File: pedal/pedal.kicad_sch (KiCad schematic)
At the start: 29 parts, among them J1 AudioJack3, J2 AudioJack3, J3 Micro SD, J4 USB_B_Micro, J5 Debug, U2 PCM3060, U3 LP2985-3.3, U4 TPS62170DSG, U5 STM32H750IBTx

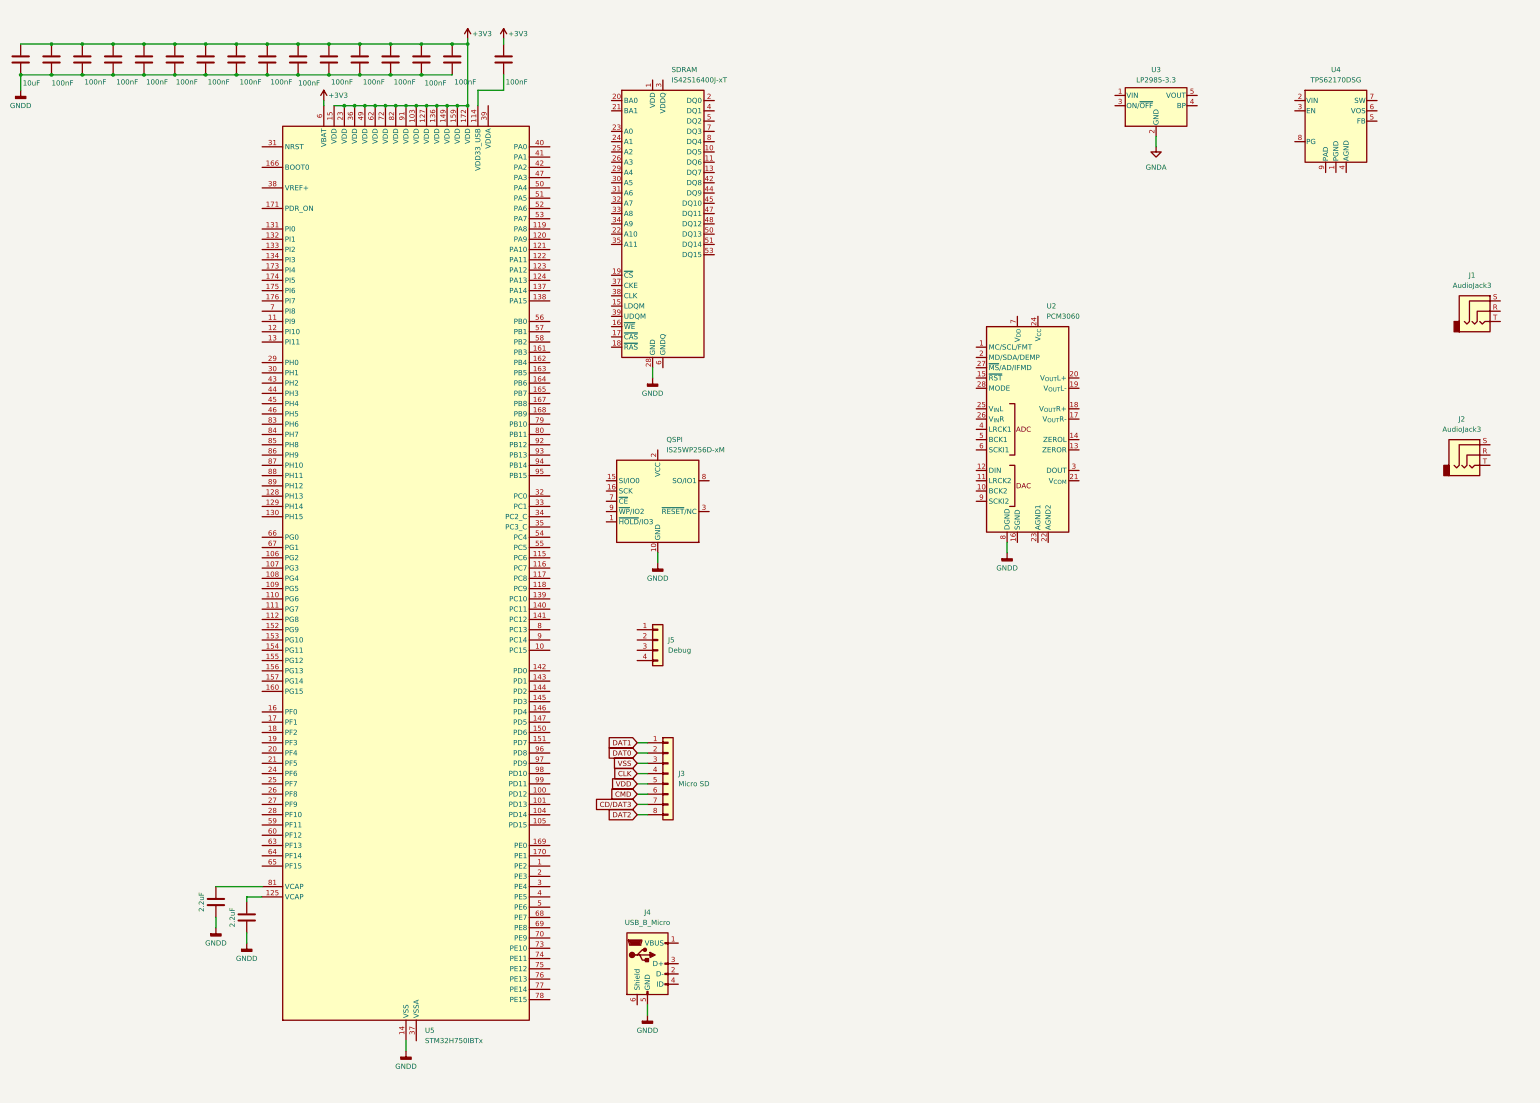
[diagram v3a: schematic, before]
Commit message: ferrite bead & buses with SDRAM
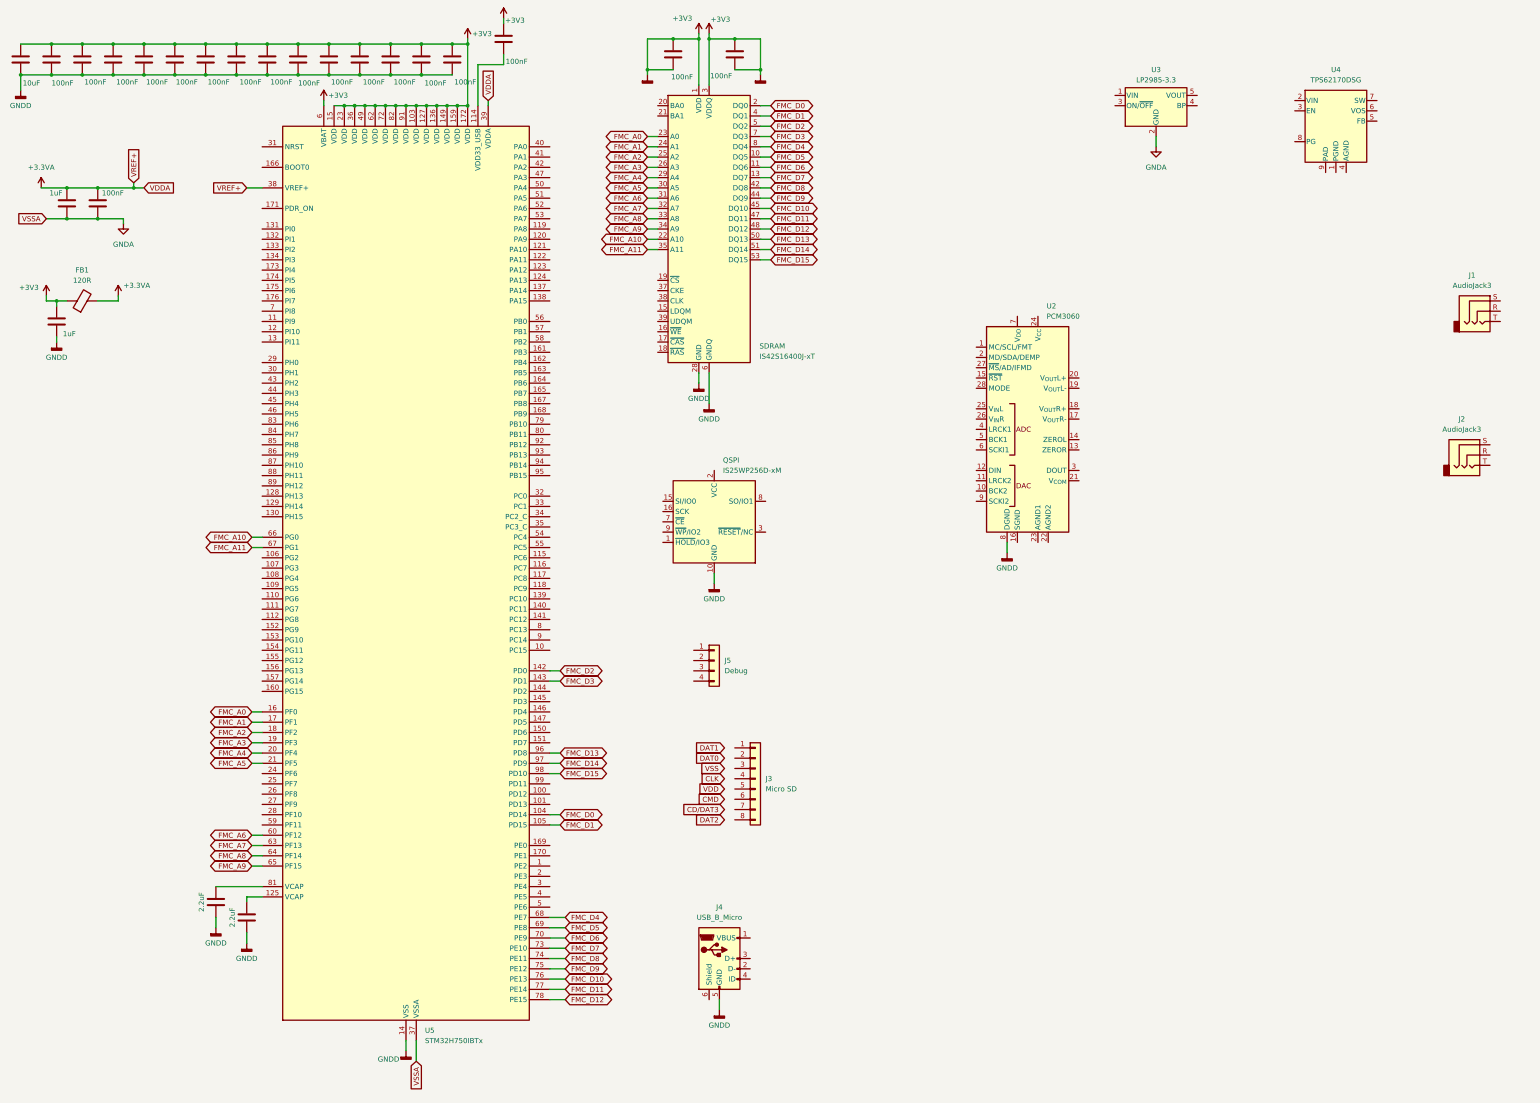
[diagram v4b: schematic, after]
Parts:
- added C19, C21: 1uF, symbol Device:C
- added C20, C22, C23: 100nF, symbol Device:C
- added FB1: 120R, symbol Device:FerriteBead
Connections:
- net GNDD is gone; now on net +3V3: C1.1, C10.2, C11.2, C12.2, C13.2, C14.2, C15.2, C16.2, C17.2, C2.1, C3.2, C4.2, C5.2, C6.2, C7.2, C8.2, C9.2, J4.5 (GND), QSPI.10 (GND), SDRAM.28 (GND), SDRAM.41 (GND), SDRAM.54 (GND), U2.8 (DGND), U5.102 (VSS), U5.113 (VSS), U5.126 (VSS), U5.135 (VSS), U5.14 (VSS), U5.148 (VSS), U5.158 (VSS), U5.22 (VSS), U5.48 (VSS), U5.61 (VSS), U5.71 (VSS), U5.90 (VSS)
- net +3V3: now also SDRAM.1 (VDD), SDRAM.12 (GNDQ), SDRAM.14 (VDD), SDRAM.27 (VDD), SDRAM.3 (VDDQ), SDRAM.43 (VDDQ), SDRAM.46 (GNDQ), SDRAM.49 (VDDQ), SDRAM.52 (GNDQ), SDRAM.6 (GNDQ), SDRAM.9 (VDDQ), C21.1, C21.2, C22.1, C22.2, C23.1, C23.2, FB1.1
- net CD/DAT3: no longer J3.7 (Pin_7)
- net CLK: no longer J3.4 (Pin_4)
- net CMD: no longer J3.6 (Pin_6)
- net DAT0: no longer J3.2 (Pin_2)
- net DAT1: no longer J3.1 (Pin_1)
- net DAT2: no longer J3.8 (Pin_8)
- net GNDA: now also U5.37 (VSSA), C19.2, C20.2
- net VDD: no longer J3.5 (Pin_5)
- net VSS: no longer J3.3 (Pin_3)
- net FMC_D5: now reaches SDRAM.10 (DQ5)
- net FMC_D5: now also U5.69 (PE8)
- net FMC_D6: now reaches SDRAM.11 (DQ6)
- net FMC_D6: now also U5.70 (PE9)
- net FMC_D7: now reaches SDRAM.13 (DQ7)
- net FMC_D7: now also U5.73 (PE10)
- net FMC_D0: now reaches SDRAM.2 (DQ0)
- net FMC_D0: now also U5.104 (PD14)
- net FMC_A10: now reaches SDRAM.22 (A10)
- net FMC_A10: now also U5.66 (PG0)
- net FMC_A0: now reaches SDRAM.23 (A0)
- net FMC_A0: now also U5.16 (PF0)
- net FMC_A1: now reaches SDRAM.24 (A1)
- net FMC_A1: now also U5.17 (PF1)
- net FMC_A2: now reaches SDRAM.25 (A2)
- net FMC_A2: now also U5.18 (PF2)
- net FMC_A3: now reaches SDRAM.26 (A3)
- net FMC_A3: now also U5.19 (PF3)
- net FMC_A4: now reaches SDRAM.29 (A4)
- net FMC_A4: now also U5.20 (PF4)
- net FMC_A5: now reaches SDRAM.30 (A5)
- net FMC_A5: now also U5.21 (PF5)
- net FMC_A6: now reaches SDRAM.31 (A6)
- net FMC_A6: now also U5.60 (PF12)
- net FMC_A7: now reaches SDRAM.32 (A7)
- net FMC_A7: now also U5.63 (PF13)
- net FMC_A8: now reaches SDRAM.33 (A8)
- net FMC_A8: now also U5.64 (PF14)
- net FMC_A9: now reaches SDRAM.34 (A9)
- net FMC_A9: now also U5.65 (PF15)
- net FMC_A11: now reaches SDRAM.35 (A11)
- net FMC_A11: now also U5.67 (PG1)
- net FMC_D1: now reaches SDRAM.4 (DQ1)
- net FMC_D1: now also U5.105 (PD15)
- net FMC_D8: now reaches SDRAM.42 (DQ8)
- net FMC_D8: now also U5.74 (PE11)
- net FMC_D9: now reaches SDRAM.44 (DQ9)
- net FMC_D9: now also U5.75 (PE12)
- net FMC_D10: now reaches SDRAM.45 (DQ10)
- net FMC_D10: now also U5.76 (PE13)
- net FMC_D11: now reaches SDRAM.47 (DQ11)
- net FMC_D11: now also U5.77 (PE14)
- net FMC_D12: now reaches SDRAM.48 (DQ12)
- net FMC_D12: now also U5.78 (PE15)
- net FMC_D2: now reaches SDRAM.5 (DQ2)
- net FMC_D2: now also U5.142 (PD0)
- net FMC_D13: now reaches SDRAM.50 (DQ13)
- net FMC_D13: now also U5.96 (PD8)
- net FMC_D14: now reaches SDRAM.51 (DQ14)
- net FMC_D14: now also U5.97 (PD9)
- net FMC_D15: now reaches SDRAM.53 (DQ15)
- net FMC_D15: now also U5.98 (PD10)
- net FMC_D3: now reaches SDRAM.7 (DQ3)
- net FMC_D3: now also U5.143 (PD1)
- net FMC_D4: now reaches SDRAM.8 (DQ4)
- net FMC_D4: now also U5.68 (PE7)
- net +3.3VA: now reaches U5.38 (VREF+)
- net +3.3VA: now also U5.39 (VDDA), C19.1, C20.1, FB1.2
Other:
- moved on the sheet: J3, J4, J5, QSPI, SDRAM

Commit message: finish wiring SDRAM
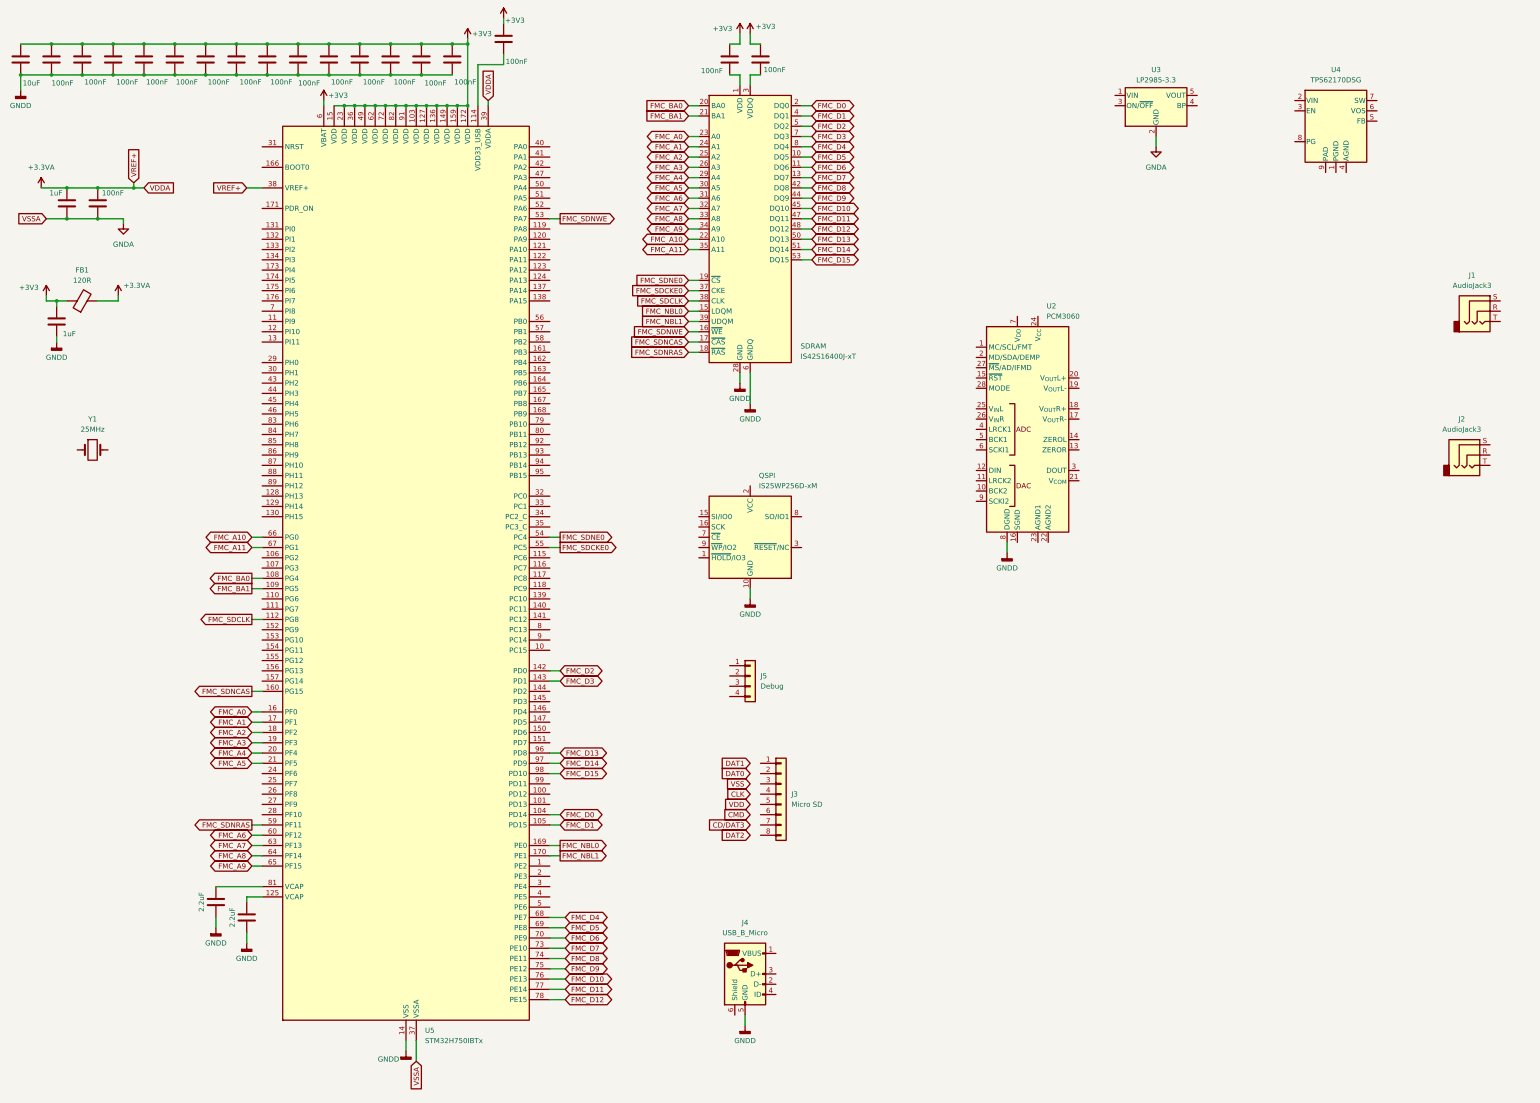
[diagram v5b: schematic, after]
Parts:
- added Y1: 25MHz, symbol Device:Crystal
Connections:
- net +3V3: no longer C1.1, C10.2, C11.2, C12.2, C13.2, C14.2, C15.2, C16.2, C17.2, C2.1, C21.2, C22.2, C23.2, C3.2, C4.2, C5.2, C6.2, C7.2, C8.2, C9.2, J4.5 (GND), QSPI.10 (GND), SDRAM.1 (VDD), SDRAM.12 (GNDQ), SDRAM.14 (VDD), SDRAM.27 (VDD), SDRAM.28 (GND), SDRAM.3 (VDDQ), SDRAM.41 (GND), SDRAM.43 (VDDQ), SDRAM.46 (GNDQ), SDRAM.49 (VDDQ), SDRAM.52 (GNDQ), SDRAM.54 (GND), SDRAM.6 (GNDQ), SDRAM.9 (VDDQ), U2.8 (DGND), U5.102 (VSS), U5.113 (VSS), U5.126 (VSS), U5.135 (VSS), U5.14 (VSS), U5.148 (VSS), U5.158 (VSS), U5.22 (VSS), U5.48 (VSS), U5.61 (VSS), U5.71 (VSS), U5.90 (VSS)
- net FMC_NBL0: now reaches SDRAM.15 (LDQM)
- net FMC_NBL0: now also U5.169 (PE0)
- net FMC_SDNWE: now reaches SDRAM.16 (~{WE})
- net FMC_SDNWE: now also U5.53 (PA7)
- net FMC_SDNCAS: now reaches SDRAM.17 (~{CAS})
- net FMC_SDNCAS: now also U5.160 (PG15)
- net FMC_SDNRAS: now reaches SDRAM.18 (~{RAS})
- net FMC_SDNRAS: now also U5.59 (PF11)
- net FMC_SDNE0: now reaches SDRAM.19 (~{CS})
- net FMC_SDNE0: now also U5.54 (PC4)
- net FMC_BA0: now reaches SDRAM.20 (BA0)
- net FMC_BA0: now also U5.108 (PG4)
- net FMC_BA1: now reaches SDRAM.21 (BA1)
- net FMC_BA1: now also U5.109 (PG5)
- net FMC_SDCKE0: now reaches SDRAM.37 (CKE)
- net FMC_SDCKE0: now also U5.55 (PC5)
- net FMC_SDCLK: now reaches SDRAM.38 (CLK)
- net FMC_SDCLK: now also U5.112 (PG8)
- net FMC_NBL1: now reaches SDRAM.39 (UDQM)
- net FMC_NBL1: now also U5.170 (PE1)
- new net: C22.2, SDRAM.1 (VDD), SDRAM.14 (VDD), SDRAM.27 (VDD)
- new net: C23.2, SDRAM.3 (VDDQ), SDRAM.43 (VDDQ), SDRAM.49 (VDDQ), SDRAM.9 (VDDQ)
- new net GNDD: C1.1, C10.2, C11.2, C12.2, C13.2, C14.2, C15.2, C16.2, C17.2, C2.1, C21.2, C3.2, C4.2, C5.2, C6.2, C7.2, C8.2, C9.2, J4.5 (GND), QSPI.10 (GND), SDRAM.12 (GNDQ), SDRAM.28 (GND), SDRAM.41 (GND), SDRAM.46 (GNDQ), SDRAM.52 (GNDQ), SDRAM.54 (GND), SDRAM.6 (GNDQ), U2.8 (DGND), U5.102 (VSS), U5.113 (VSS), U5.126 (VSS), U5.135 (VSS), U5.14 (VSS), U5.148 (VSS), U5.158 (VSS), U5.22 (VSS), U5.48 (VSS), U5.61 (VSS), U5.71 (VSS), U5.90 (VSS)
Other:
- moved on the sheet: J3, J4, J5, QSPI, SDRAM

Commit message: add external clock
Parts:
- added C24, C25: 18pF, symbol Device:C
- added R1: 10R, symbol Device:R
- added R2: 47R, symbol Device:R
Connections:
- net FMC_SDCLK: now also R1.1; no longer U5.112 (PG8)
- net GNDD: now also C24.1, C25.1
- net OSC_OUT: now reaches Y1.1
- net OSC_OUT: now also C25.2, R2.2
- net OSC_IN: now reaches Y1.2
- net OSC_IN: now also U5.29 (PH0), C24.2
- net at U5.30 (PH1): now also R2.1
- new net: R1.2, U5.112 (PG8)
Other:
- moved on the sheet: Y1

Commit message: update LDO
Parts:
- removed U3: LP2985-3.3, Package_TO_SOT_SMD:SOT-23-5, symbol Regulator_Linear:LP2985-3.3
- added C26: 10nF, symbol Device:C
- added C27: 1.0uF, symbol Device:C
- added C28: 4.7uF, symbol Device:C
- added U1: LP2985-1.8, Package_TO_SOT_SMD:SOT-23-5, symbol Regulator_Linear:LP2985-1.8
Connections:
- net +3V3: now also C27.1, U1.1 (VIN), U1.3 (ON/~{OFF})
- net GNDA: now also C26.2, C27.2, C28.2, U1.2 (GND)
- net QUADSPI_CLK: now reaches QSPI.16 (SCK)
- new net: C26.1, U1.4 (BP)
- new net +1V8: C28.1, U1.5 (VOUT)
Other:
- moved on the sheet: QSPI

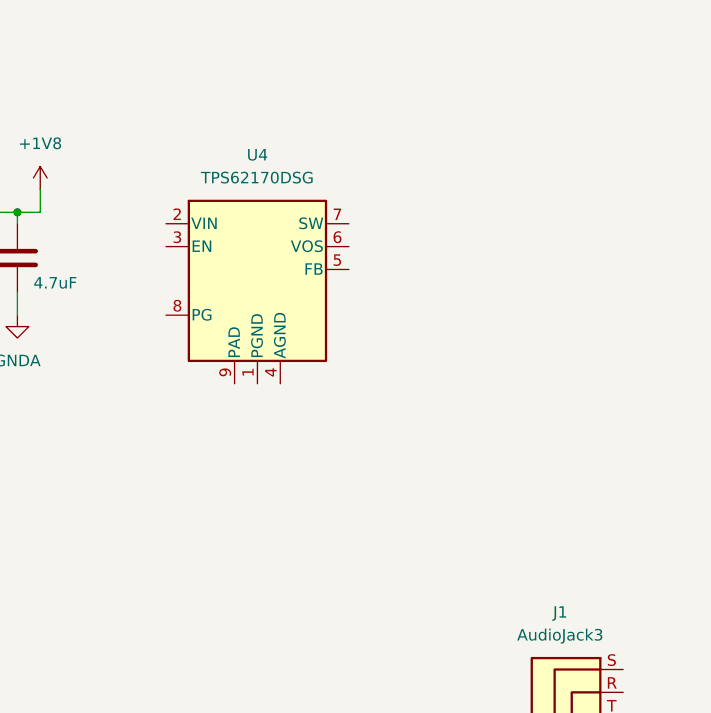
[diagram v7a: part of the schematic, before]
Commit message: update TPS62
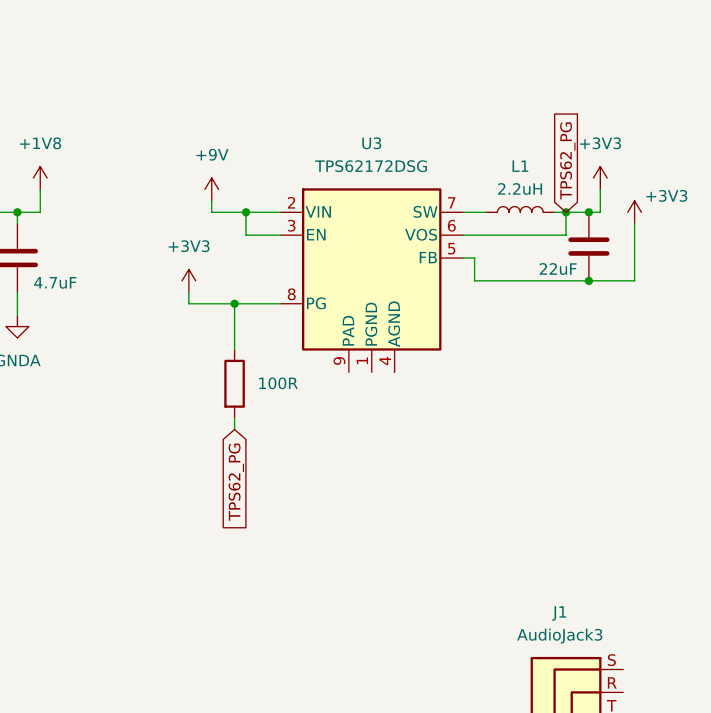
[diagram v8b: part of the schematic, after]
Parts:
- removed U4: TPS62170DSG, Package_SON:WSON-8-1EP_2x2mm_P0.5mm_EP0.9x1.6mm_ThermalVias, symbol Regulator_Switching:TPS62170DSG
- added C29: 22uF, symbol Device:C
- added L1: 2.2uH, symbol Device:L
- added R3: 100R, symbol Device:R
- added U3: TPS62172DSG, Package_SON:WSON-8-1EP_2x2mm_P0.5mm_EP0.9x1.6mm_ThermalVias, symbol Regulator_Switching:TPS62172DSG
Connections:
- net +3V3: now also C29.1, C29.2, L1.2, R3.1, R3.2, U3.5 (FB), U3.6 (VOS), U3.8 (PG)
- new net: L1.1, U3.7 (SW)
- new net +9V: U3.2 (VIN), U3.3 (EN)
